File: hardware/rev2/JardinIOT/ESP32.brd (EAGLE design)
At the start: 160 x 100 mm, 5 parts, among them IC1 7815TV

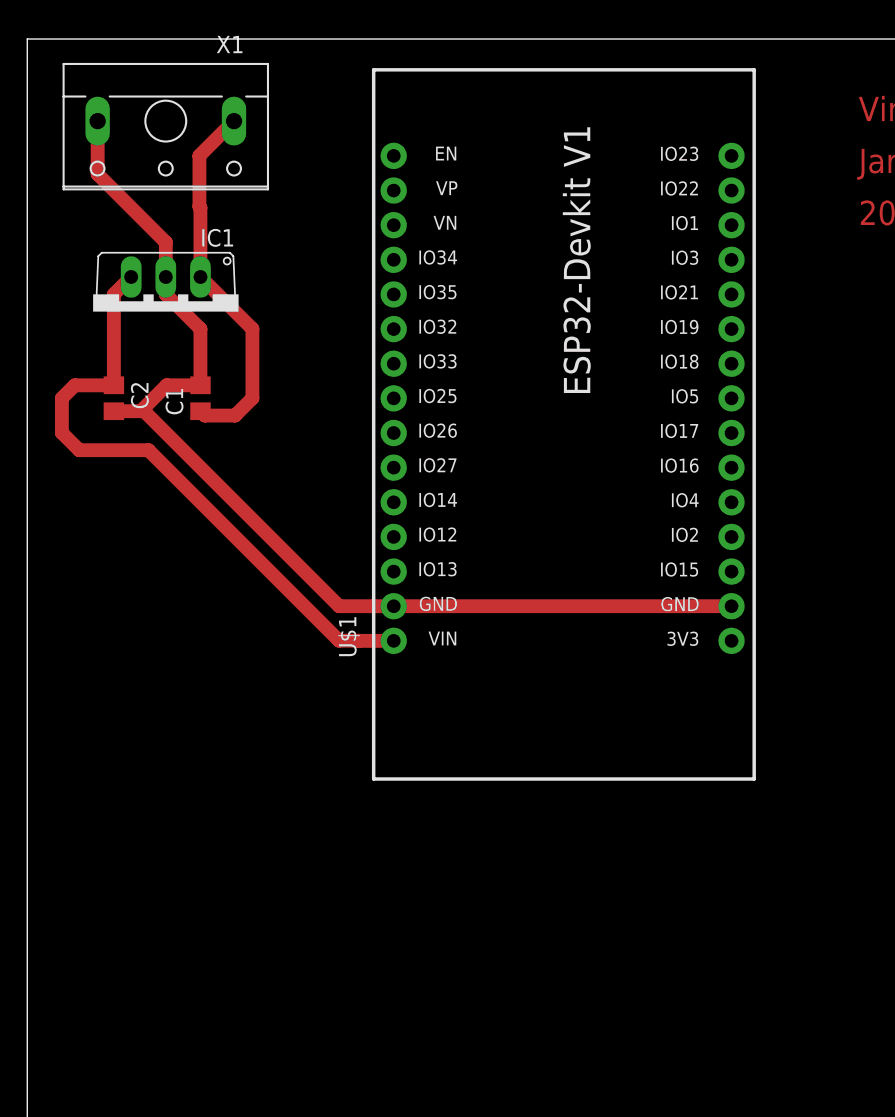
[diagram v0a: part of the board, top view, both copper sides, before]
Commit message: Ajout de bouton multi-utilitaires sur la plaquette.
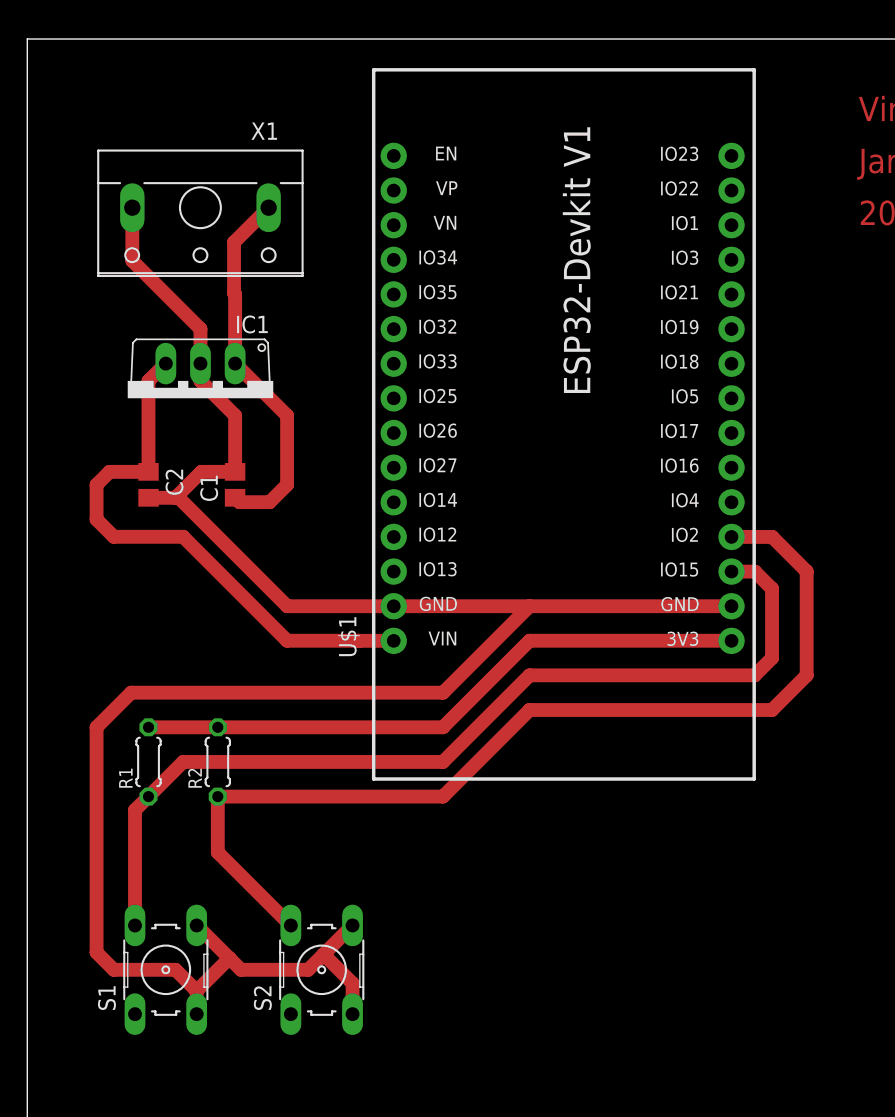
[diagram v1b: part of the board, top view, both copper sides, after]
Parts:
- added R1, R2: 220Ω, rcl:0204/5
- added S1, S2: (no value), switch-omron:B3F-10XX
- moved IC1 6.84 mm to (12.7, 73.7)
- moved C1 6.84 mm to (15.2, 67.3)
- moved C2 6.84 mm to (8.89, 67.3)
- moved X1 6.84 mm to (12.7, 86.4)
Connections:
- removed net N$2: U$1.1
- new net 3V3: R1.2, R2.2, U$1.1
- new net N$1: R1.1, S1.1, S1.2, U$1.3
- new net N$3: R2.1, S2.1, S2.2, U$1.4
- net GND: now also S1.3, S1.4, S2.3, S2.4
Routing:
- net GND: track 78.9 -> 158.9 mm
- net N$3: track 0.00 -> 72.7 mm
- net N$1: track 0.00 -> 68.4 mm
- net 3V3: track 0.00 -> 45.4 mm
- net 5V_VCC: track 45.9 -> 40.7 mm

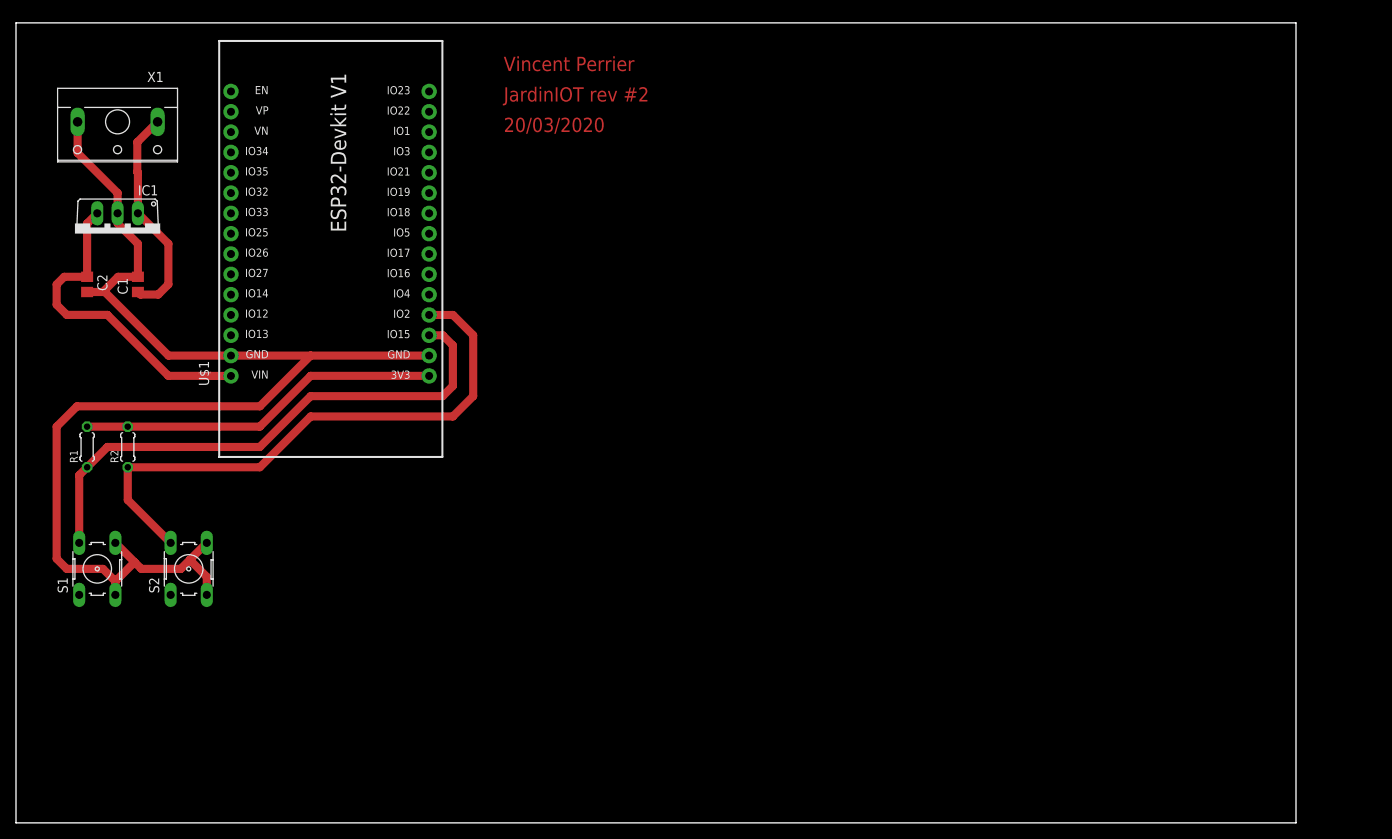
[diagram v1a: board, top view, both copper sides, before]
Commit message: Ajout des borniers à vis pour les capteurs et actionneurs
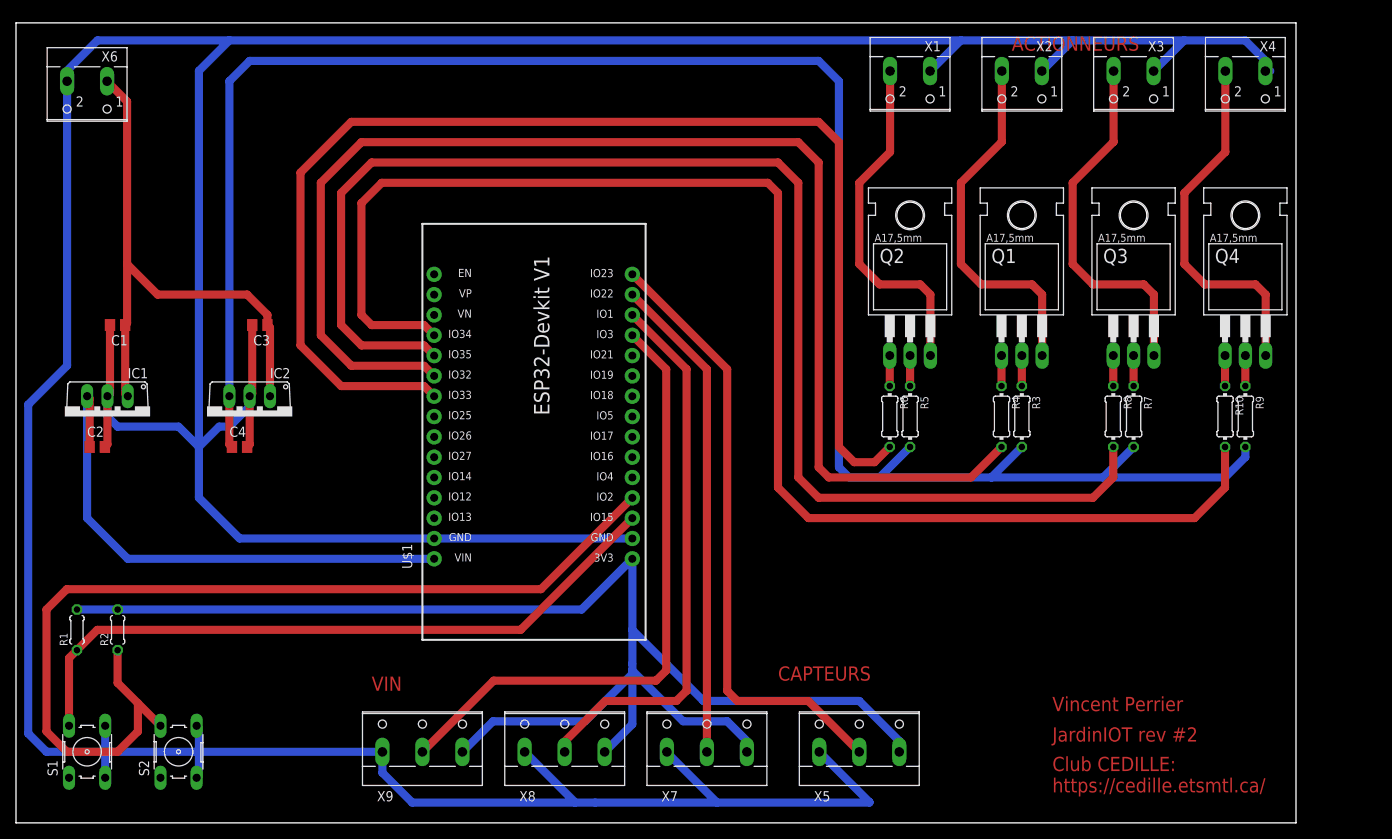
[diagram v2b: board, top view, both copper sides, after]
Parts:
- added C3: 0.33µF, rcl:C0805
- added C4: 0.1µF, rcl:C0805
- added IC2: 7812TV, linear:TO220V
- added Q1, Q2, Q3, Q4: BD243, transistor-npn:TO220
- added R10, R4, R6, R8: 24 OHM, rcl:0204/7
- added R3, R5, R7, R9: 12 OHM, rcl:0204/7
- added X2, X3, X4, X6: (no value), con-wago-500:W237-102
- added X5, X7, X8, X9: (no value), con-wago-500:W237-103
- X1: device con-wago-500:W237-113 -> con-wago-500:W237-102
- moved X1 99.3 mm to (111.8, 92.7)
- moved U$1 34.2 mm to (63.5, 55.9)
- moved R1 22.9 mm to (7.62, 24.1)
- moved R2 22.9 mm to (12.7, 24.1)
- moved IC1 22.9 mm to (11.4, 50.8)
- moved S1 22.9 mm to (8.89, 8.89)
- moved S2 22.9 mm to (20.3, 8.89)
- moved C2 20.4 mm to (10.2, 47.0), turned to 0 degrees
- moved C1 5.68 mm to (12.7, 62.2), turned to 180 degrees
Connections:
- removed net 20V_VCC: C1.1, IC1.1, X1.1
- new net 12V_VCC: C4.1, IC2.3, R3.2, R5.2, R7.2, R9.2
- new net 20VDC: C1.1, C3.1, IC1.1, IC2.1, X6.1
- new net N$10: Q3.2, R7.1
- new net N$11: Q3.1, R8.1
- new net N$12: Q4.3, X4.2
- new net N$13: Q4.2, R9.1
- new net N$14: Q4.1, R10.1
- new net N$15: R10.2, U$1.19
- new net N$16: U$1.15, X5.2
- new net N$17: R8.2, U$1.20
- new net N$18: R6.2, U$1.22
- new net N$19: R4.2, U$1.21
- new net N$2: Q1.3, X2.2
- new net N$20: U$1.14, X7.2
- new net N$21: U$1.13, X8.2
- new net N$22: U$1.12, X9.2
- new net N$4: Q1.2, R3.1
- new net N$5: Q1.1, R4.1
- new net N$6: Q2.3, X1.2
- new net N$7: Q2.2, R5.1
- new net N$8: Q2.1, R6.1
- new net N$9: Q3.3, X3.2
- net 3V3: now also X5.3, X7.3, X8.3, X9.3
- net GND: now also C3.2, C4.2, IC2.2, X1.1, X2.1, X3.1, X4.1, X5.1, X6.2, X7.1, X8.1, X9.1; no longer X1.2
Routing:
- net GND: track 158.9 -> 577.4 mm
- net 12V_VCC: track 0.00 -> 242.2 mm
- net N$15: track 0.00 -> 178.7 mm
- net N$17: track 0.00 -> 171.6 mm
- net N$19: track 0.00 -> 163.8 mm
- net N$18: track 0.00 -> 158.0 mm
- net 3V3: track 45.4 -> 182.7 mm
- net N$22: track 0.00 -> 78.4 mm
- net N$16: track 0.00 -> 76.6 mm
- net 20VDC: track 0.00 -> 71.1 mm
- net N$21: track 0.00 -> 68.9 mm
- net N$20: track 0.00 -> 61.0 mm
- net N$3: track 72.7 -> 123.0 mm
- net N$2: track 0.00 -> 45.6 mm
- net N$9: track 0.00 -> 45.6 mm
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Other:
- board text added: "ACTIONNEURS"
- board text added: "CAPTEURS"
- board text added: "Club CEDILLE: https://cedille.etsmtl.ca/"
- board text added: "VIN"
- board text removed: "20/03/2020"
